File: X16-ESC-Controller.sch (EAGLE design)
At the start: 23 parts, among them J6 TMMH-110-05-F-D, U1 AZ1117IH-3.3TRG1

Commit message: 11/17/23
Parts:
- TP1, TP2, TP3: value (none) -> TESTPOINT_5.04MM; device SparkFun-Connectors:CONN_01 -> X16-ExtraComponents:TESTPOINT_5.04MM
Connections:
- net 3V3: now also TP1.TP; no longer TP1.1
- net 5.2V: now also TP2.TP; no longer TP2.1
- net GND: now also TP3.TP; no longer TP3.1
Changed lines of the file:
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@@
 <part name="J6" library="TMMH-110-05-F-D" deviceset="TMMH-110-05-F-D" device=""/>
 <part name="GND9" library="SparkFun-PowerSymbols" library_urn="urn:adsk.eagle:library:530" deviceset="GND" device=""/>
-<part name="TP1" library="SparkFun-Connectors" library_urn="urn:adsk.eagle:library:513" deviceset="CONN_01" device="" package3d_urn="urn:adsk.eagle:package:38028/2"/>
-<part name="TP2" library="SparkFun-Connectors" library_urn="urn:adsk.eagle:library:513" deviceset="CONN_01" device="" package3d_urn="urn:adsk.eagle:package:38028/2"/>
-<part name="TP3" library="SparkFun-Connectors" library_urn="urn:adsk.eagle:library:513" deviceset="CONN_01" device="" package3d_urn="urn:adsk.eagle:package:38028/2"/>
+<part name="TP1" library="X16-ExtraComponents" deviceset="TESTPOINT_5.04MM" device=""/>
+<part name="TP2" library="X16-ExtraComponents" deviceset="TESTPOINT_5.04MM" device=""/>
+<part name="TP3" library="X16-ExtraComponents" deviceset="TESTPOINT_5.04MM" device=""/>
 </parts>
 <sheets>
@@
 <attribute name="VALUE" x="60.96" y="84.074" size="1.778" layer="96" font="vector" rot="R180" align="top-center"/>
 </instance>
-<instance part="TP1" gate="J1" x="259.08" y="203.2" smashed="yes" rot="R180">
-<attribute name="VALUE" x="261.62" y="208.026" size="1.778" layer="96" font="vector" rot="R180"/>
-<attribute name="NAME" x="261.62" y="200.152" size="1.778" layer="95" font="vector" rot="R180"/>
-</instance>
-<instance part="TP2" gate="J1" x="259.08" y="190.5" smashed="yes" rot="R180">
-<attribute name="VALUE" x="261.62" y="195.326" size="1.778" layer="96" font="vector" rot="R180"/>
-<attribute name="NAME" x="261.62" y="187.452" size="1.778" layer="95" font="vector" rot="R180"/>
-</instance>
-<instance part="TP3" gate="J1" x="259.08" y="177.8" smashed="yes" rot="R180">
-<attribute name="VALUE" x="261.62" y="182.626" size="1.778" layer="96" font="vector" rot="R180"/>
-<attribute name="NAME" x="261.62" y="174.752" size="1.778" layer="95" font="vector" rot="R180"/>
+<instance part="TP1" gate="G$1" x="254" y="203.2" smashed="yes" rot="R180">
+<attribute name="NAME" x="255.27" y="199.644" size="1.778" layer="95" rot="R180"/>
+</instance>
+<instance part="TP2" gate="G$1" x="254" y="190.5" smashed="yes" rot="R180">
+<attribute name="NAME" x="255.27" y="186.944" size="1.778" layer="95" rot="R180"/>
+</instance>
+<instance part="TP3" gate="G$1" x="254" y="177.8" smashed="yes" rot="R180">
+<attribute name="NAME" x="255.27" y="174.244" size="1.778" layer="95" rot="R180"/>
 </instance>
 </instances>
@@
 </segment>
 <segment>
-<pinref part="TP3" gate="J1" pin="1"/>
-<wire x1="251.46" y1="177.8" x2="241.3" y2="177.8" width="0.1524" layer="91"/>
+<wire x1="251.46" y1="177.8" x2="250.698" y2="177.8" width="0.1524" layer="91"/>
 <label x="241.3" y="177.8" size="1.778" layer="95" rot="R180" xref="yes"/>
+<pinref part="TP3" gate="G$1" pin="TP"/>
+<wire x1="250.698" y1="177.8" x2="241.3" y2="177.8" width="0.1524" layer="91"/>
+<junction x="250.698" y="177.8"/>
 </segment>
 </net>
@@
 </segment>
 <segment>
-<pinref part="TP1" gate="J1" pin="1"/>
-<wire x1="251.46" y1="203.2" x2="241.3" y2="203.2" width="0.1524" layer="91"/>
+<wire x1="251.46" y1="203.2" x2="250.698" y2="203.2" width="0.1524" layer="91"/>
 <label x="241.3" y="203.2" size="1.778" layer="95" rot="R180" xref="yes"/>
+<pinref part="TP1" gate="G$1" pin="TP"/>
+<wire x1="250.698" y1="203.2" x2="241.3" y2="203.2" width="0.1524" layer="91"/>
+<junction x="250.698" y="203.2"/>
 </segment>
 </net>
@@
 </segment>
 <segment>
-<pinref part="TP2" gate="J1" pin="1"/>
-<wire x1="251.46" y1="190.5" x2="241.3" y2="190.5" width="0.1524" layer="91"/>
+<wire x1="251.46" y1="190.5" x2="250.698" y2="190.5" width="0.1524" layer="91"/>
 <label x="241.3" y="190.5" size="1.778" layer="95" rot="R180" xref="yes"/>
-</segment>
-</net>
+<pinref part="TP2" gate="G$1" pin="TP"/>
+<wire x1="250.698" y1="190.5" x2="241.3" y2="190.5" width="0.1524" layer="91"/>
+<junction x="250.698" y="190.5"/>
+</segment>
+</net>

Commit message: 12/16/2023
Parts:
- removed J4: (no value), SparkFun-Connectors:CONN_05LOCK
- removed J5: (no value), SparkFun-Connectors:CONN_02
- added JP1: (no value), X16-ExtraComponents:TEST_PIN-1X5
- added JP2: (no value), X16-ExtraComponents:TEST_PIN-1X2
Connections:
- net 3V3: now also JP1.5, JP2.2, R1.2; no longer J4.5, J5.2, R1.1
- net GND: now also JP1.3, JP2.1; no longer J4.3, J5.1
- net NRST: now also JP1.1, R1.1; no longer J4.1, R1.2
- net SWCLK: now also JP1.4; no longer J4.4
- net SWDIO: now also JP1.2; no longer J4.2
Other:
- moved on the sheet: C5, C7, D2, J1, J2, J6, R1, R6, TP1, TP2, TP3, U1

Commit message: 12/6/2023 pt2
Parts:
- renumbered JP1 to .., JP2 to .
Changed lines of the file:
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@@
 <part name="J2" library="SparkFun-Connectors" library_urn="urn:adsk.eagle:library:513" deviceset="CONN_06" device="NO_SILK_NO_POP" package3d_urn="urn:adsk.eagle:package:38130/2"/>
 <part name="R1" library="SparkFun-Resistors" library_urn="urn:adsk.eagle:library:532" deviceset="2.55KOHM" device="-0603-1/10W-1%" package3d_urn="urn:adsk.eagle:package:41389018/1" value="1k"/>
-<part name="JP1" library="X16-ExtraComponents" deviceset="TEST_PIN-1X5" device="" package3d_urn="urn:adsk.eagle:package:22469/2"/>
-<part name="JP2" library="X16-ExtraComponents" deviceset="TEST_PIN-1X2" device="" package3d_urn="urn:adsk.eagle:package:22435/2"/>
+<part name=".." library="X16-ExtraComponents" deviceset="TEST_PIN-1X5" device="" package3d_urn="urn:adsk.eagle:package:22469/2"/>
+<part name="." library="X16-ExtraComponents" deviceset="TEST_PIN-1X2" device="" package3d_urn="urn:adsk.eagle:package:22435/2"/>
 </parts>
 <sheets>
@@
 <attribute name="VALUE" x="15.24" y="159.004" size="1.778" layer="96" font="vector" rot="R180" align="top-center"/>
 </instance>
-<instance part="JP1" gate="A" x="187.96" y="134.62" smashed="yes" rot="R180">
+<instance part=".." gate="A" x="187.96" y="134.62" smashed="yes" rot="R180">
 <attribute name="NAME" x="194.31" y="126.365" size="1.778" layer="95" rot="R180"/>
 <attribute name="VALUE" x="194.31" y="144.78" size="1.778" layer="96" rot="R180"/>
 </instance>
-<instance part="JP2" gate="G$1" x="233.68" y="142.24" smashed="yes" rot="R180">
+<instance part="." gate="G$1" x="233.68" y="142.24" smashed="yes" rot="R180">
 <attribute name="NAME" x="240.03" y="136.525" size="1.778" layer="95" rot="R180"/>
 <attribute name="VALUE" x="240.03" y="147.32" size="1.778" layer="96" rot="R180"/>
@@
 </segment>
 <segment>
-<pinref part="JP1" gate="A" pin="3"/>
+<pinref part=".." gate="A" pin="3"/>
 <wire x1="193.04" y1="134.62" x2="205.74" y2="134.62" width="0.1524" layer="91"/>
 <label x="203.2" y="134.62" size="1.778" layer="95" align="bottom-right"/>
 </segment>
 <segment>
-<pinref part="JP2" gate="G$1" pin="1"/>
+<pinref part="." gate="G$1" pin="1"/>
 <wire x1="238.76" y1="139.7" x2="251.46" y2="139.7" width="0.1524" layer="91"/>
 <label x="248.92" y="139.7" size="1.778" layer="95" align="bottom-right"/>
@@
 </segment>
 <segment>
-<pinref part="JP1" gate="A" pin="2"/>
+<pinref part=".." gate="A" pin="2"/>
 <wire x1="193.04" y1="132.08" x2="205.74" y2="132.08" width="0.1524" layer="91"/>
 <label x="203.2" y="132.08" size="1.778" layer="95" align="bottom-right"/>
@@
 </segment>
 <segment>
-<pinref part="JP1" gate="A" pin="1"/>
+<pinref part=".." gate="A" pin="1"/>
 <wire x1="193.04" y1="129.54" x2="205.74" y2="129.54" width="0.1524" layer="91"/>
 <label x="203.2" y="129.54" size="1.778" layer="95" align="bottom-right"/>
@@
 </segment>
 <segment>
-<pinref part="JP1" gate="A" pin="5"/>
+<pinref part=".." gate="A" pin="5"/>
 <wire x1="193.04" y1="139.7" x2="205.74" y2="139.7" width="0.1524" layer="91"/>
 <label x="203.2" y="139.7" size="1.778" layer="95" align="bottom-right"/>
 </segment>
 <segment>
-<pinref part="JP2" gate="G$1" pin="2"/>
+<pinref part="." gate="G$1" pin="2"/>
 <wire x1="238.76" y1="142.24" x2="251.46" y2="142.24" width="0.1524" layer="91"/>
 <label x="248.92" y="142.24" size="1.778" layer="95" align="bottom-right"/>
@@
 </segment>
 <segment>
-<pinref part="JP1" gate="A" pin="4"/>
+<pinref part=".." gate="A" pin="4"/>
 <wire x1="193.04" y1="137.16" x2="205.74" y2="137.16" width="0.1524" layer="91"/>
 <label x="203.2" y="137.16" size="1.778" layer="95" align="bottom-right"/>

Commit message: 12/06/2023 pt3
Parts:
- D1, D2: device SparkFun-LED:LED-GREEN-0603-WE -> SparkFun-LED:LED-GREEN0805-PG
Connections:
- removed net N$16: D2.A, R6.2
- new net N$1: D2.C, R6.2
- net 3V3: now also D2.A; no longer D2.C
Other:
- moved on the sheet: D2
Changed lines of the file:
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@@
 <part name="C4" library="SparkFun-Capacitors" library_urn="urn:adsk.eagle:library:510" deviceset="4.7PF" device="-0603-50V-5%" package3d_urn="urn:adsk.eagle:package:41385090/1" value="0.1uF"/>
 <part name="R2" library="SparkFun-Resistors" library_urn="urn:adsk.eagle:library:532" deviceset="2.55KOHM" device="-0603-1/10W-1%" package3d_urn="urn:adsk.eagle:package:41389018/1" value="1k"/>
-<part name="D1" library="SparkFun-LED" library_urn="urn:adsk.eagle:library:529" deviceset="LED-GREEN" device="-0603-WE" package3d_urn="urn:adsk.eagle:package:39354/2" value="Green"/>
+<part name="D1" library="SparkFun-LED" library_urn="urn:adsk.eagle:library:529" deviceset="LED-GREEN" device="0805-PG" package3d_urn="urn:adsk.eagle:package:41389318/1" value="Green"/>
 <part name="GND7" library="SparkFun-PowerSymbols" library_urn="urn:adsk.eagle:library:530" deviceset="GND" device=""/>
 <part name="J1" library="SparkFun-Connectors" library_urn="urn:adsk.eagle:library:513" deviceset="CONN_06" device="NO_SILK_NO_POP" package3d_urn="urn:adsk.eagle:package:38130/2"/>
-<part name="D2" library="SparkFun-LED" library_urn="urn:adsk.eagle:library:529" deviceset="LED-GREEN" device="-0603-WE" package3d_urn="urn:adsk.eagle:package:39354/2" value="Green"/>
+<part name="D2" library="SparkFun-LED" library_urn="urn:adsk.eagle:library:529" deviceset="LED-GREEN" device="0805-PG" package3d_urn="urn:adsk.eagle:package:41389318/1" value="Green"/>
 <part name="R6" library="SparkFun-Resistors" library_urn="urn:adsk.eagle:library:532" deviceset="2.55KOHM" device="-0603-1/10W-1%" package3d_urn="urn:adsk.eagle:package:41389018/1" value="150"/>
 <part name="GND10" library="SparkFun-PowerSymbols" library_urn="urn:adsk.eagle:library:530" deviceset="GND" device=""/>
@@
 <instance part="D1" gate="G$1" x="96.52" y="205.74" smashed="yes" rot="R180">
 <attribute name="NAME" x="99.949" y="210.312" size="1.778" layer="95" font="vector" rot="R270"/>
-<attribute name="VALUE" x="94.615" y="210.312" size="1.778" layer="96" font="vector" rot="R270" align="top-left"/>
 </instance>
 <instance part="GND7" gate="1" x="96.52" y="218.44" smashed="yes" rot="R180">
@@
 <attribute name="NAME" x="154.94" y="203.708" size="1.778" layer="95" font="vector"/>
 </instance>
-<instance part="D2" gate="G$1" x="195.58" y="86.36" smashed="yes" rot="R180">
-<attribute name="NAME" x="199.009" y="90.932" size="1.778" layer="95" font="vector" rot="R270"/>
+<instance part="D2" gate="G$1" x="195.58" y="88.9" smashed="yes">
+<attribute name="NAME" x="192.151" y="84.328" size="1.778" layer="95" font="vector" rot="R90"/>
 </instance>
 <instance part="R6" gate="G$1" x="195.58" y="78.74" smashed="yes" rot="R90">
@@
 <wire x1="96.52" y1="132.08" x2="96.52" y2="127" width="0.1524" layer="91"/>
 <label x="96.52" y="124.46" size="1.778" layer="95" rot="R90"/>
-</segment>
-</net>
-<net name="N$16" class="0">
-<segment>
-<pinref part="R6" gate="G$1" pin="2"/>
-<pinref part="D2" gate="G$1" pin="A"/>
 </segment>
 </net>
@@
 </segment>
 <segment>
-<wire x1="195.58" y1="91.44" x2="195.58" y2="93.98" width="0.1524" layer="91"/>
-<pinref part="D2" gate="G$1" pin="C"/>
-<label x="193.04" y="93.98" size="1.778" layer="95"/>
-</segment>
-<segment>
 <wire x1="220.98" y1="198.12" x2="220.218" y2="198.12" width="0.1524" layer="91"/>
 <label x="210.82" y="198.12" size="1.778" layer="95" rot="R180" xref="yes"/>
@@
 <wire x1="238.76" y1="142.24" x2="251.46" y2="142.24" width="0.1524" layer="91"/>
 <label x="248.92" y="142.24" size="1.778" layer="95" align="bottom-right"/>
+</segment>
+<segment>
+<pinref part="D2" gate="G$1" pin="A"/>
+<wire x1="195.58" y1="91.44" x2="195.58" y2="96.52" width="0.1524" layer="91"/>
+<label x="195.58" y="96.52" size="1.778" layer="95"/>
 </segment>
 </net>
@@
 </segment>
 </net>
+<net name="N$1" class="0">
+<segment>
+<pinref part="R6" gate="G$1" pin="2"/>
+<pinref part="D2" gate="G$1" pin="C"/>
+</segment>
+</net>

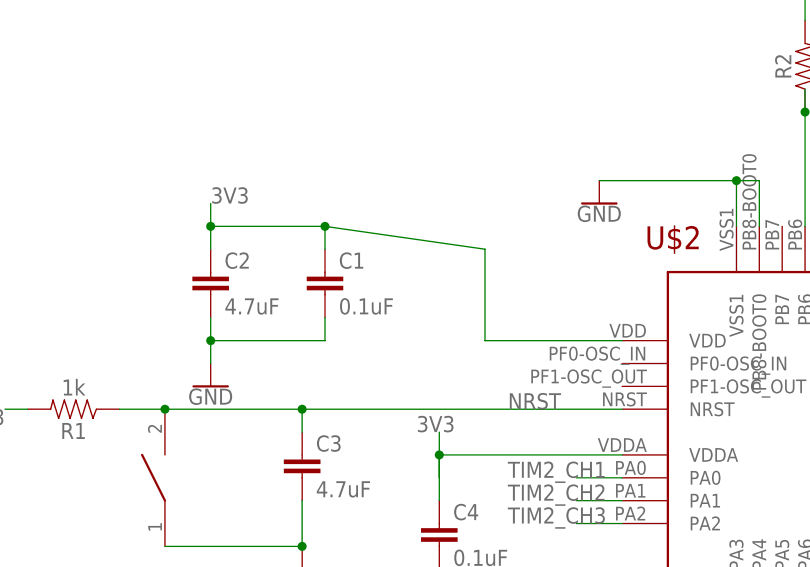
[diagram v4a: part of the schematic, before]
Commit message: increased text size + minor changes to trace routing
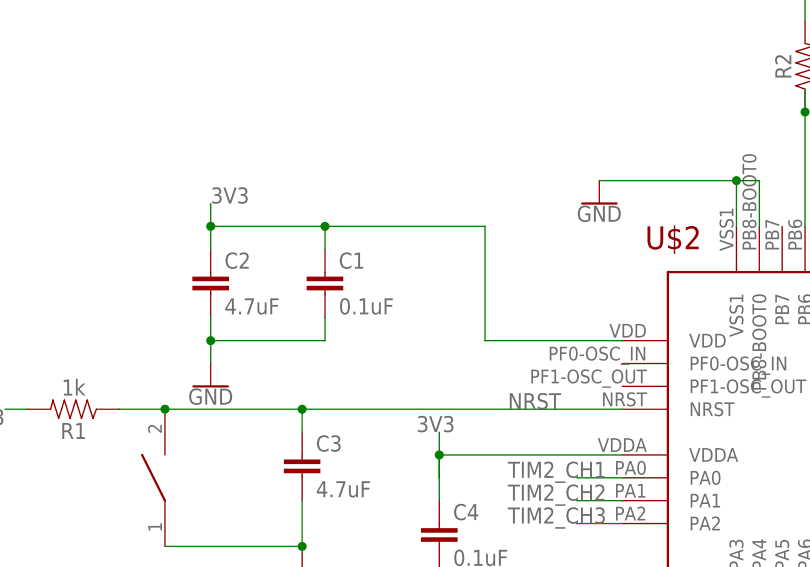
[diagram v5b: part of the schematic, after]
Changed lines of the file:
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@@
 <pinref part="U$2" gate="G$1" pin="VDD"/>
 <wire x1="76.2" y1="165.1" x2="60.96" y2="165.1" width="0.1524" layer="91"/>
-<wire x1="60.96" y1="165.1" x2="60.96" y2="175.26" width="0.1524" layer="91"/>
-<wire x1="60.96" y1="175.26" x2="43.18" y2="177.8" width="0.1524" layer="91"/>
+<wire x1="60.96" y1="165.1" x2="60.96" y2="177.8" width="0.1524" layer="91"/>
+<wire x1="60.96" y1="177.8" x2="43.18" y2="177.8" width="0.1524" layer="91"/>
 <pinref part="C1" gate="G$1" pin="1"/>
 <wire x1="43.18" y1="177.8" x2="30.48" y2="177.8" width="0.1524" layer="91"/>

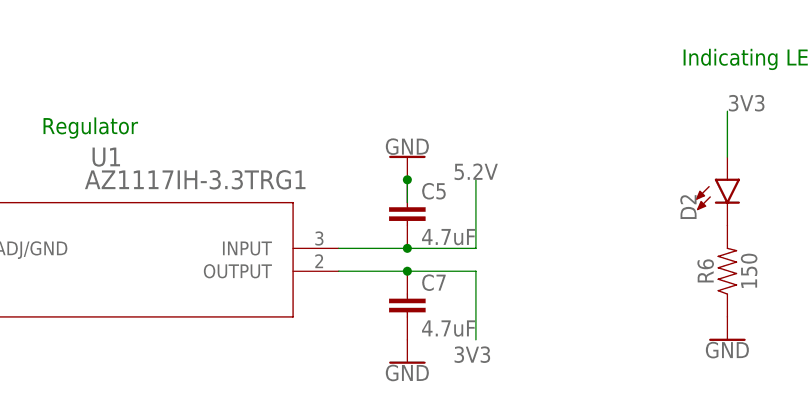
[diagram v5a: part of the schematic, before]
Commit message: fixed LDO thermals and pad 4, updated LDO caps to datasheet recommended, cleaned up silkscreen
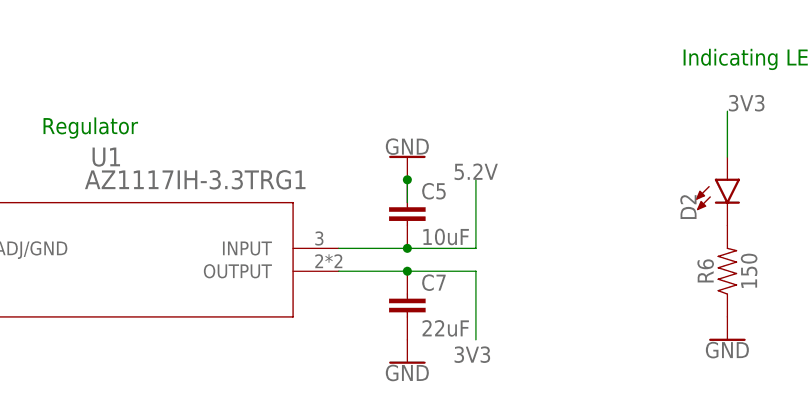
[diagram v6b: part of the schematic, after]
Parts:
- C5: value 4.7uF -> 10uF
- C7: value 4.7uF -> 22uF
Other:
- moved on the sheet: U1
